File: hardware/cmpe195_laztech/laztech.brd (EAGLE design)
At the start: 68.6 x 61 mm, 28 parts

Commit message: Pre-route checkpoint.
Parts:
- moved C2 34.2 mm to (35.6, 24.1), turned to 270 degrees
- moved C8 33.8 mm to (29.2, 22.9), turned to 180 degrees
- moved C10 33.5 mm to (33.0, 24.1), turned to 270 degrees
- moved C6 31.0 mm to (29.2, 25.4), turned to 0 degrees
- moved U$2 25.0 mm to (33.0, 30.5), turned to 0 degrees
- moved C4 22.9 mm to (39.4, 41.9), turned to 270 degrees
- moved C13 15.7 mm to (33.0, 14.0)
- moved U$8 15.7 mm to (38.1, 16.5)
- moved R1 14.5 mm to (40.6, 11.4)
- moved R2 14.5 mm to (36.8, 11.4)
- moved R3 14.5 mm to (36.8, 8.89)
- moved C12 13.7 mm to (26.7, 35.6), turned to 180 degrees
- moved R6 13.7 mm to (34.3, 43.2), turned to 90 degrees
- moved C5 13.3 mm to (45.7, 25.4)
- moved C7 13.0 mm to (45.7, 22.9)
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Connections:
- net N$1: now also U$5.10; no longer U$5.9
- net N$2: now also U$5.9; no longer U$5.10
- net N$5: now also U$2.15; no longer U$2.18
- net N$6: now also U$2.18; no longer U$2.15
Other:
- board size 68.6 x 61 mm -> 66 x 61 mm
- board text added: "CUT OUT"

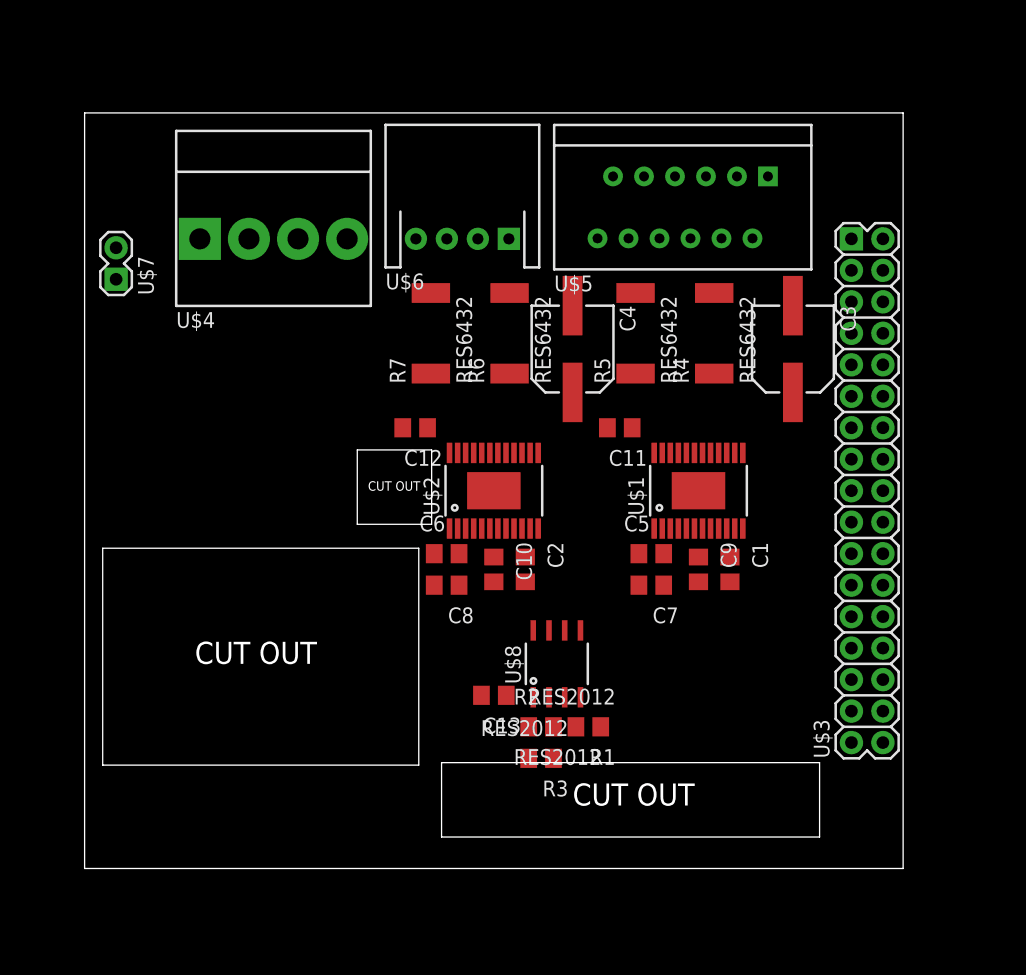
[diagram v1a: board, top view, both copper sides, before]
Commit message: Routed stepper motor outputs.
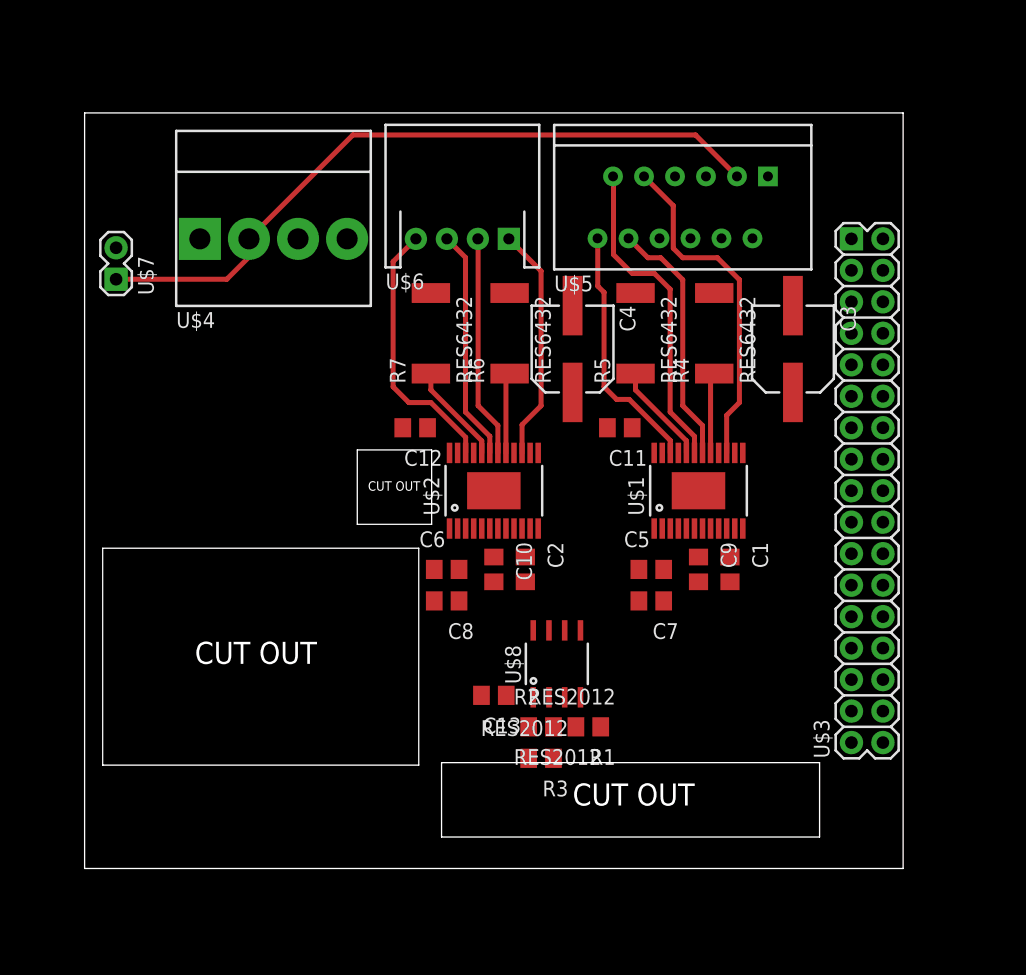
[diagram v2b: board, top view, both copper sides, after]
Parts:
- moved C5 1.27 mm to (45.7, 24.1)
- moved C6 1.27 mm to (29.2, 24.1)
- moved C7 1.27 mm to (45.7, 21.6)
- moved C8 1.27 mm to (29.2, 21.6)
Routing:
- net +5V: track 0.00 -> 57.2 mm
- net N$2: track 0.00 -> 27.6 mm
- net N$3: track 0.00 -> 26.1 mm
- net N$8: track 0.00 -> 21.5 mm
- net N$1: track 0.00 -> 20.4 mm
- net N$4: track 0.00 -> 20.3 mm
- net N$5: track 0.00 -> 19.0 mm
- net N$7: track 0.00 -> 18.7 mm
- net N$6: track 0.00 -> 17.9 mm
- net N$40: track 0.00 -> 8.10 mm
- net N$35: track 0.00 -> 8.10 mm
- net N$38: track 0.00 -> 6.52 mm
- net N$9: track 0.00 -> 6.52 mm

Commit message: Partial layout. Still need to route signals to uCPU.
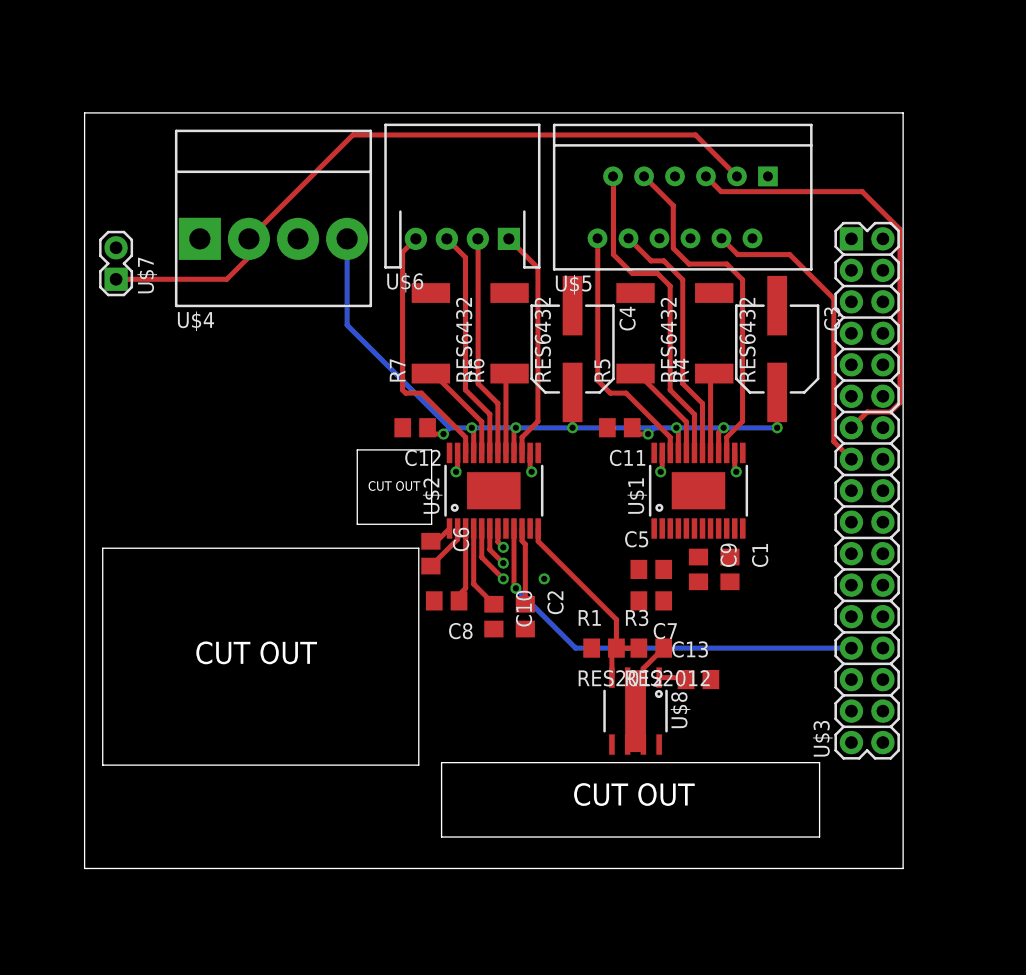
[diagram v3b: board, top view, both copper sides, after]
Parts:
- removed R2: RES2012, laztech_parts:R2012
- moved C13 16.6 mm to (49.5, 15.2), turned to 0 degrees
- moved R3 12.6 mm to (45.7, 17.8), turned to 0 degrees
- moved U$8 7.41 mm to (44.5, 12.7), turned to 180 degrees
- moved R1 6.48 mm to (41.9, 17.8), turned to 0 degrees
- moved C10 3.81 mm to (33.0, 20.3)
- moved C2 3.81 mm to (35.6, 20.3)
- moved C6 1.80 mm to (27.9, 25.4), turned to 270 degrees
- moved C3 1.27 mm to (55.9, 41.9)
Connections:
- net +24V: now also C3.2, C4.2; no longer C3.1, C4.1
- net GND: now also C3.1, C4.1; no longer C3.2, C4.2
- net N$34: no longer R2.1
- net VREF: no longer R2.2
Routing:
- net +24V: track 0.00 -> 65.9 mm, vias 0 -> 8
- net N$10: track 0.00 -> 36.2 mm
- net N$22: track 0.00 -> 34.0 mm, vias 0 -> 1
- net N$11: track 0.00 -> 24.6 mm
- net VREF: track 0.00 -> 16.6 mm
- net N$34: track 0.00 -> 15.1 mm
- net N$26: track 0.00 -> 6.78 mm
- net +3V3: track 0.00 -> 6.22 mm
- net N$29: track 0.00 -> 6.06 mm
- net N$14: track 0.00 -> 4.78 mm
- net N$28: track 0.00 -> 3.92 mm
- net N$13: track 0.00 -> 3.24 mm
- net N$27: track 0.00 -> 1.93 mm
- net N$21: track 0.00 -> 1.70 mm
- net N$19: track 0.00 -> 1.58 mm
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
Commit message: Vref routed.
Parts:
- moved C1 3.81 mm to (52.1, 20.3)
- moved C9 3.81 mm to (49.5, 20.3)
- moved C5 1.80 mm to (44.5, 25.4), turned to 270 degrees
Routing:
- net +24V: track 65.9 -> 119.8 mm, vias 8 -> 9
- net VREF: track 16.6 -> 35.4 mm
- net N$25: track 0.00 -> 16.6 mm, vias 0 -> 1
- net N$34: track 15.1 -> 3.06 mm
- net N$30: track 0.00 -> 6.78 mm
- net +3V3: track 6.22 -> 12.4 mm
- net N$33: track 0.00 -> 6.06 mm
- net N$17: track 0.00 -> 4.78 mm
- net N$32: track 0.00 -> 3.92 mm
- net N$18: track 0.00 -> 3.24 mm
- net N$31: track 0.00 -> 1.93 mm
- net N$23: track 0.00 -> 1.70 mm
- net N$16: track 0.00 -> 1.58 mm
- net N$15: track 0.00 -> 1.58 mm
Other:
- board text added: "LazTech Motor Driver (rev. 1) Spring/Fall 2016 Irlanda Altamirano Yasmine Jamjoum Alex Kennedy"

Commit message: Finished first round of routing.
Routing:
- net +3V3: track 12.4 -> 93.4 mm, vias 0 -> 4
- net N$20: track 1.58 -> 43.5 mm, vias 0 -> 3
- net N$13: track 3.24 -> 44.8 mm, vias 0 -> 1
- net N$15: track 1.58 -> 38.3 mm, vias 0 -> 3
- net N$14: track 4.78 -> 41.2 mm, vias 0 -> 2
- net N$19: track 1.58 -> 34.9 mm, vias 0 -> 3
- net N$21: track 1.70 -> 34.4 mm, vias 0 -> 1
- net N$12: track 1.58 -> 34.1 mm, vias 0 -> 2
- net N$18: track 3.24 -> 31.0 mm, vias 0 -> 1
- net N$17: track 4.78 -> 32.0 mm, vias 0 -> 1
- net N$16: track 1.58 -> 24.4 mm, vias 0 -> 1
- net N$24: track 1.58 -> 20.7 mm, vias 0 -> 2
- net N$23: track 1.70 -> 20.3 mm, vias 0 -> 1
- net GND: track 0.00 -> 9.64 mm, vias 0 -> 33
- added copper zone on layer 1, net GND
- added copper zone on layer 16, net GND
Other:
- board size 66 x 61 mm -> 68.8 x 61 mm

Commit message: Last commit for tonight's work.
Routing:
- net N$34: track 3.06 -> 5.60 mm
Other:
- board size 68.8 x 61 mm -> 68.6 x 61 mm
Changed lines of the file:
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@@
 <layer number="35" name="tGlue" color="7" fill="4" visible="no" active="yes"/>
 <layer number="36" name="bGlue" color="7" fill="5" visible="no" active="yes"/>
-<layer number="37" name="tTest" color="7" fill="1" visible="yes" active="yes"/>
-<layer number="38" name="bTest" color="7" fill="1" visible="yes" active="yes"/>
+<layer number="37" name="tTest" color="7" fill="1" visible="no" active="yes"/>
+<layer number="38" name="bTest" color="7" fill="1" visible="no" active="yes"/>
 <layer number="39" name="tKeepout" color="4" fill="11" visible="no" active="yes"/>
 <layer number="40" name="bKeepout" color="1" fill="11" visible="no" active="yes"/>
 <layer number="41" name="tRestrict" color="4" fill="10" visible="no" active="yes"/>
 <layer number="42" name="bRestrict" color="1" fill="10" visible="no" active="yes"/>
-<layer number="43" name="vRestrict" color="2" fill="10" visible="yes" active="yes"/>
+<layer number="43" name="vRestrict" color="2" fill="10" visible="no" active="yes"/>
 <layer number="44" name="Drills" color="7" fill="1" visible="yes" active="yes"/>
 <layer number="45" name="Holes" color="7" fill="1" visible="yes" active="yes"/>
@@
 <board>
 <plain>
-<wire x1="0" y1="0" x2="68.834" y2="0" width="0" layer="20"/>
-<wire x1="68.834" y1="0" x2="68.58" y2="60.96" width="0" layer="20"/>
+<wire x1="0" y1="0" x2="68.58" y2="0" width="0" layer="20"/>
+<wire x1="68.58" y1="0" x2="68.58" y2="60.96" width="0" layer="20"/>
 <wire x1="68.58" y1="60.96" x2="0" y2="60.96" width="0" layer="20"/>
 <wire x1="0" y1="60.96" x2="0" y2="0" width="0" layer="20"/>
@@
 <wire x1="46.72" y1="17.78" x2="45.085" y2="16.145" width="0.4064" layer="1"/>
 <wire x1="45.085" y1="16.145" x2="45.085" y2="15.4" width="0.4064" layer="1"/>
-<wire x1="45.085" y1="15.4" x2="43.815" y2="15.4" width="0" layer="19" extent="1-1"/>
+<wire x1="45.085" y1="15.4" x2="43.815" y2="15.4" width="0.254" layer="1"/>
+<wire x1="43.815" y1="10" x2="45.085" y2="10" width="0.254" layer="1"/>
 <wire x1="43.815" y1="10" x2="43.815" y2="15.4" width="0" layer="19" extent="1-1"/>
-<wire x1="45.085" y1="10" x2="43.815" y2="10" width="0" layer="19" extent="1-1"/>
 </signal>
 <signal name="VREF">

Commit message: Messed up and made the sch and brd not consistant. Trying to roll back.
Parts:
- moved C8 0.25 mm to (29.2, 21.3)
- moved C1 0.25 mm to (52.3, 20.3)
- moved C2 0.25 mm to (35.8, 20.3)
- moved C6 0.25 mm to (28.2, 25.4)
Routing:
- net GND: track 9.64 -> 6.91 mm, vias 33 -> 0
- net +24V: track 119.8 -> 120.4 mm
- net VREF: track 35.4 -> 35.9 mm
- removed copper zone on layer 1, net GND
- removed copper zone on layer 16, net GND
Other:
- board text added: "CUT OUT (OK to notch to edge if needed.)"

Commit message: Got brd and sch back on track.
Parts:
- moved C8 0.25 mm to (29.2, 21.6)
- moved C1 0.25 mm to (52.1, 20.3)
- moved C2 0.25 mm to (35.6, 20.3)
- moved C6 0.25 mm to (27.9, 25.4)
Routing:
- net +24V: track 120.4 -> 119.8 mm
- net VREF: track 35.9 -> 35.4 mm
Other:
- board text removed: "CUT OUT (OK to notch to edge if needed.)"
